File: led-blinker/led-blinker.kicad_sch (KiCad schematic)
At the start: 3 parts

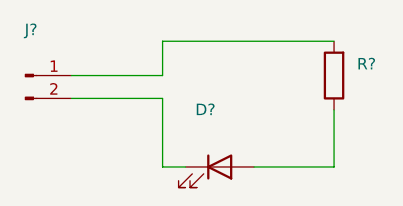
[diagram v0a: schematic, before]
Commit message: Give component numbering
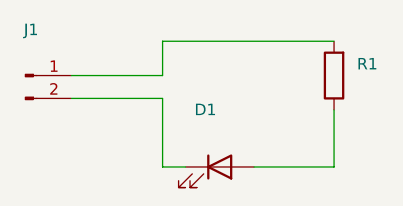
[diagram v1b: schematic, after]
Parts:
- gave numbers to parts that had none: 3
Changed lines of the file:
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@@
   (symbol (lib_id "Device:R") (at 101.6 48.26 180) (unit 1)
     (in_bom yes) (on_board yes) (fields_autoplaced)
-    (property "Reference" "R?" (id 0) (at 104.14 46.9899 0)
+    (property "Reference" "R1" (id 0) (at 104.14 46.9899 0)
       (effects (font (size 1.27 1.27)) (justify right))
     )
@@
   (symbol (lib_id "Device:LED") (at 88.9 58.42 0) (unit 1)
     (in_bom yes) (on_board yes) (fields_autoplaced)
-    (property "Reference" "D?" (id 0) (at 87.3125 52.07 0))
+    (property "Reference" "D1" (id 0) (at 87.3125 52.07 0))
     (property "Value" "" (id 1) (at 87.3125 54.61 0))
     (property "Footprint" "" (id 2) (at 88.9 58.42 0)
@@
   (symbol (lib_id "Connector:Conn_01x02_Male") (at 67.31 48.26 0) (unit 1)
     (in_bom yes) (on_board yes) (fields_autoplaced)
-    (property "Reference" "J?" (id 0) (at 67.945 43.18 0))
+    (property "Reference" "J1" (id 0) (at 67.945 43.18 0))
     (property "Value" "" (id 1) (at 67.945 45.72 0))
     (property "Footprint" "" (id 2) (at 67.31 48.26 0)
@@
   (symbol_instances
     (path "/65d5c78a-4863-4a6e-8ee9-7f7694e5dd47"
-      (reference "D?") (unit 1) (value "LED") (footprint "")
+      (reference "D1") (unit 1) (value "LED") (footprint "")
     )
     (path "/f9329c69-2177-408e-ab28-0f41ea23d485"
-      (reference "J?") (unit 1) (value "Conn_01x02_Male") (footprint "")
+      (reference "J1") (unit 1) (value "Conn_01x02_Male") (footprint "")
     )
     (path "/275b6416-db29-42cc-9307-bf426917c3b4"
-      (reference "R?") (unit 1) (value "R") (footprint "")
+      (reference "R1") (unit 1) (value "R") (footprint "")
     )
   )
